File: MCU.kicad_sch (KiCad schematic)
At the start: 24 parts, among them J5 Micro_SD_Card, U4 EFM32GG332, Y1 Crystal_GND23

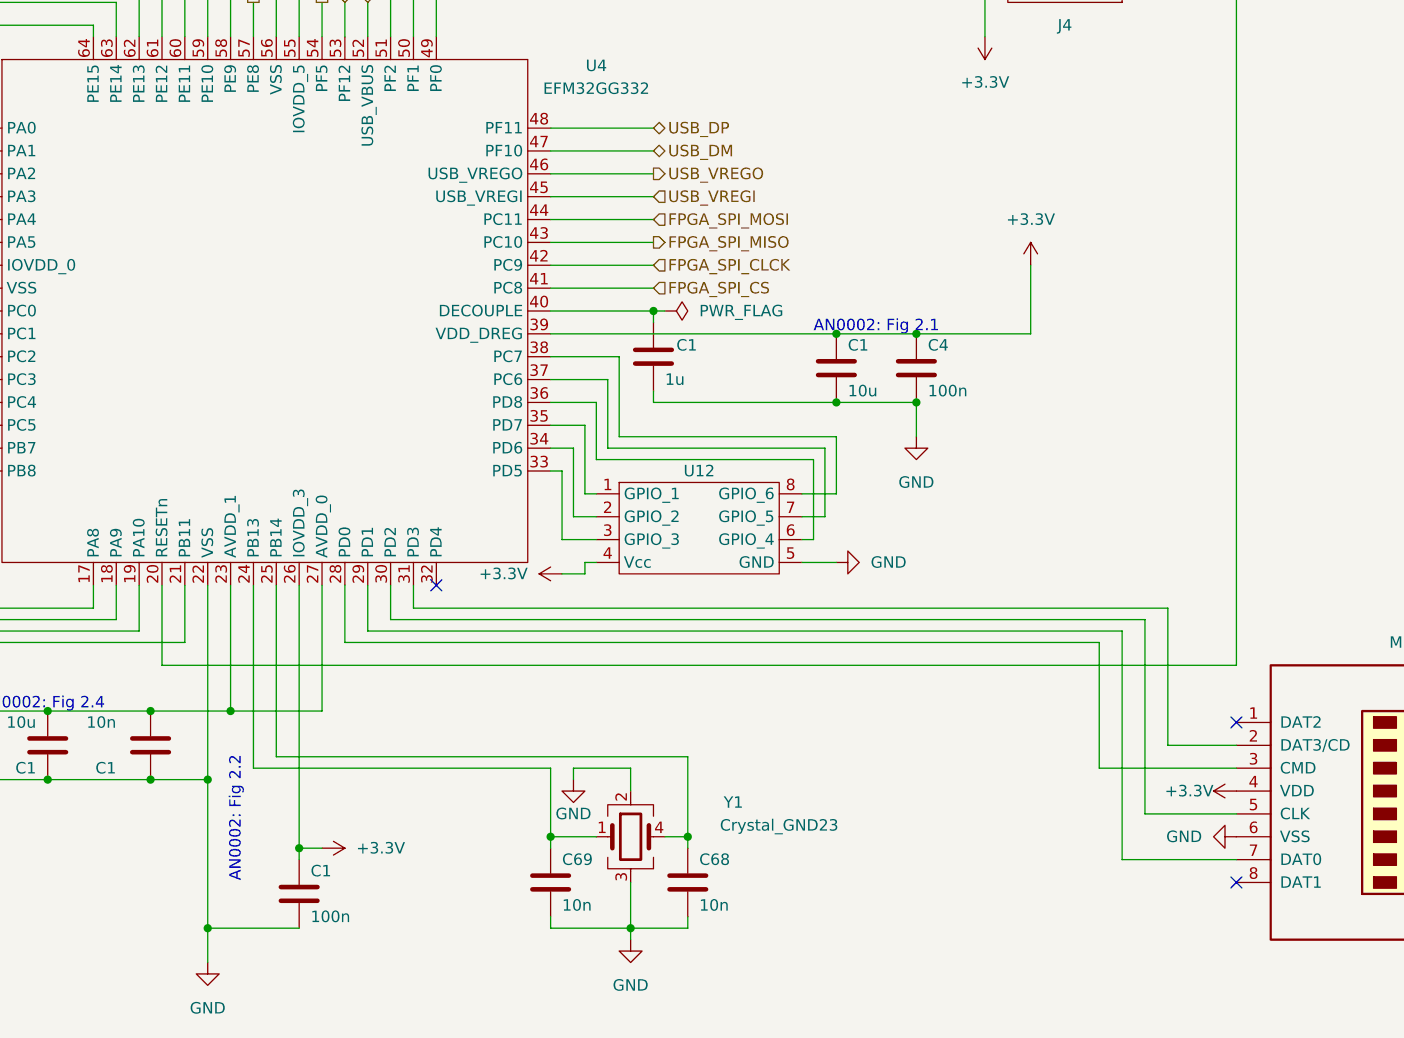
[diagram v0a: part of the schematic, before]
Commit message: Added Pullup resistors
And disconnected unused USB_volt ports
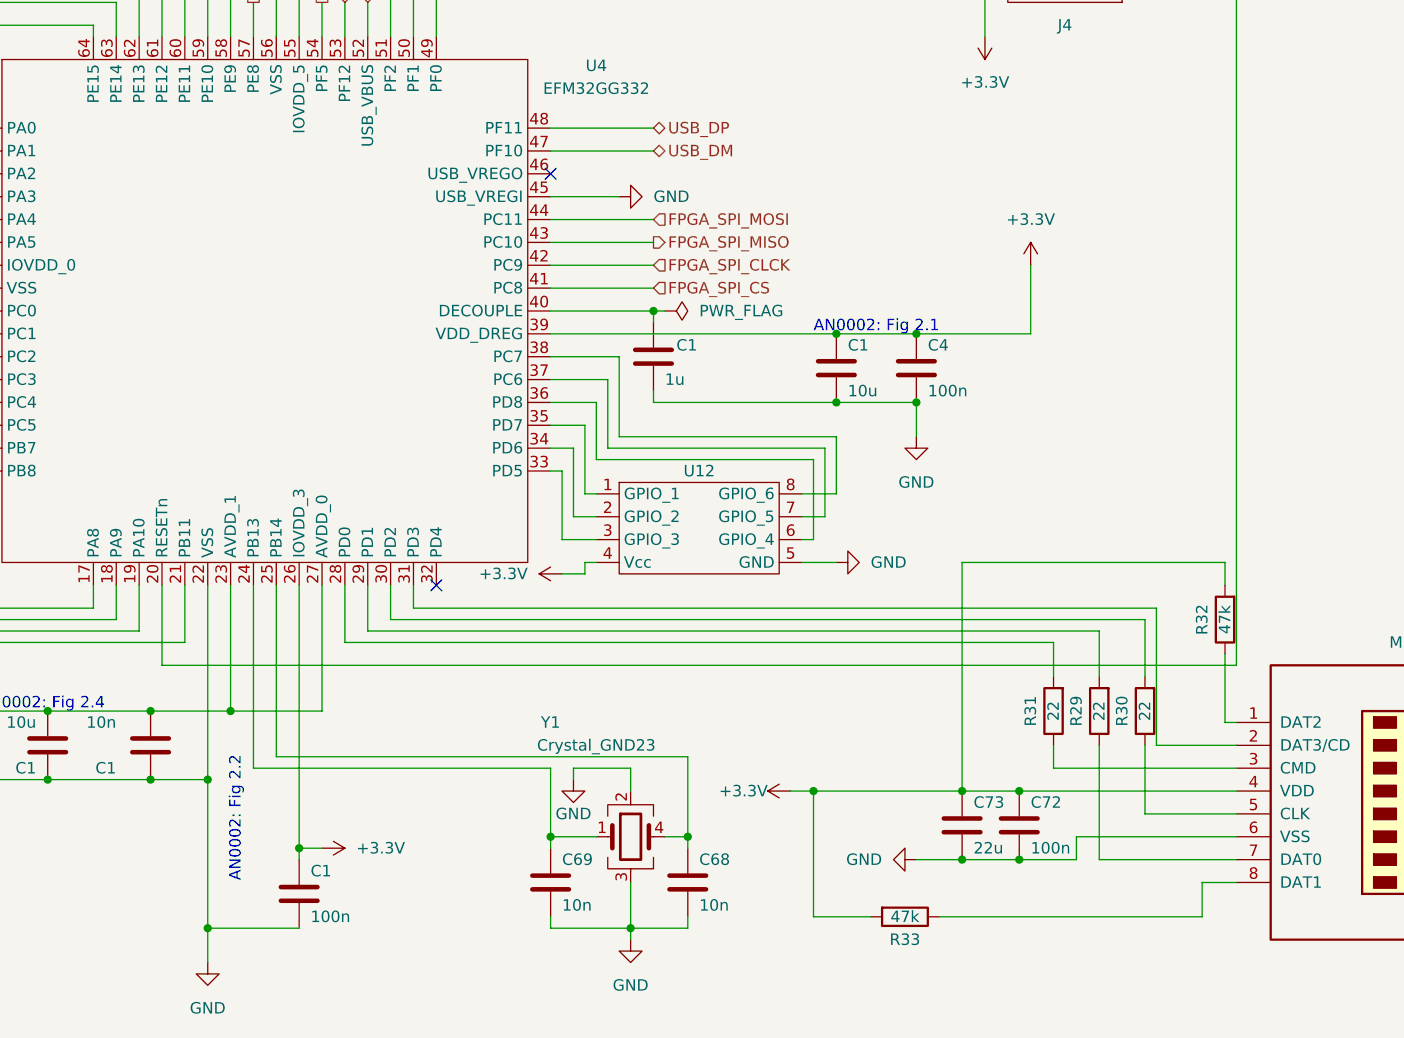
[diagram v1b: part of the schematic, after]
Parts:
- added C72: 100n, symbol Device:C
- added C73: 22u, symbol Device:C
- added R29, R30, R31: 22, symbol Device:R
- added R32, R33: 47k, symbol Device:R
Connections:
- net USB_VREGI is gone; now on net GND: U4.45 (USB_VREGI)
- net +3.3V: now also C72.1, C73.1, R32.2, R33.2
- net GND: now also C72.2, C73.2
- net at U4.28 (PD0): now also R31.2; no longer J5.3 (CMD)
- net at J5.7 (DAT0): now also R29.1; no longer U4.29 (PD1)
- net at U4.30 (PD2): now also R30.2; no longer J5.5 (CLK)
- net at J5.1 (DAT2): now also R32.1
- net at J5.8 (DAT1): now also R33.1
- net USB_VREGO: no longer names the net of U4.46 (USB_VREGO)
- new net: R29.2, U4.29 (PD1)
- new net: R21.1, U11.2 (R4), U13.2 (R4)
- new net: J5.3 (CMD), R31.1
- new net: J5.5 (CLK), R30.1
- no-connect marks 3 -> 2

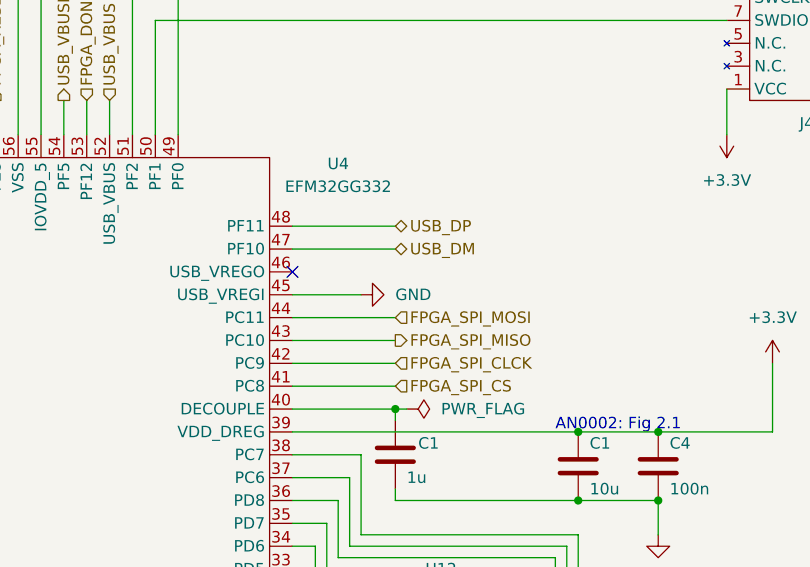
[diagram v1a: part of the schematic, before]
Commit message: Fixed mistake in USB_A connection
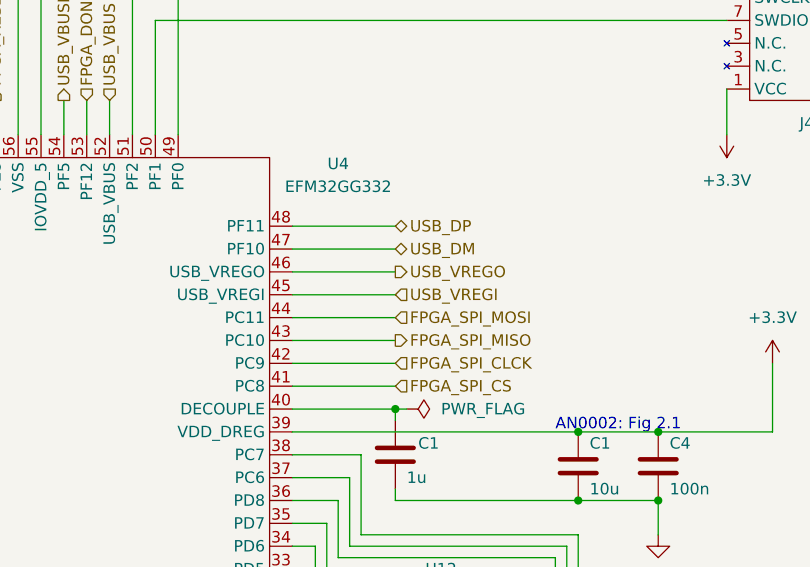
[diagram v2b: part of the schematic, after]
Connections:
- net GND: no longer U4.45 (USB_VREGI)
- net USB_VREGO: now reaches U4.46 (USB_VREGO)
- new net: R21.1, U11.2 (R4), U13.2 (R4)
- new net USB_VREGI: U4.45 (USB_VREGI)
- no-connect marks 2 -> 1
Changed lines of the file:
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@@
   )
   (no_connect (at 149.86 124.46))
-  (no_connect (at 162.56 78.74))
   (wire (pts (xy 46.99 113.03) (xy 63.5 113.03))
     (stroke (width 0) (type default))
@@
     (stroke (width 0) (type default))
   )
-  (wire (pts (xy 162.56 81.28) (xy 170.18 81.28))
+  (wire (pts (xy 162.56 81.28) (xy 173.99 81.28))
     (stroke (width 0) (type default))
   )
@@
   )
   (wire (pts (xy 134.62 153.67) (xy 134.62 154.94))
+    (stroke (width 0) (type default))
+  )
+  (wire (pts (xy 162.56 78.74) (xy 173.99 78.74))
     (stroke (width 0) (type default))
   )
@@
     (effects (font (size 1.27 1.27)) (justify left))
   )
+  (hierarchical_label "USB_VREGI" (shape input) (at 173.99 81.28 0) (fields_autoplaced)
+    (effects (font (size 1.27 1.27)) (justify left))
+  )
   (hierarchical_label "FPGA_RESET" (shape output) (at 129.54 59.69 90) (fields_autoplaced)
     (effects (font (size 1.27 1.27)) (justify left))
@@
   (hierarchical_label "Button 3" (shape input) (at 93.98 78.74 180) (fields_autoplaced)
     (effects (font (size 1.27 1.27)) (justify right))
+  )
+  (hierarchical_label "USB_VREGO" (shape output) (at 173.99 78.74 0) (fields_autoplaced)
+    (effects (font (size 1.27 1.27)) (justify left))
   )
   (hierarchical_label "FPGA_SPI_MOSI" (shape input) (at 173.99 83.82 0) (fields_autoplaced)
@@
         )
       )
-    )
-  )
-  (symbol (lib_id "power:GND") (at 170.18 81.28 90) (unit 1)
-    (in_bom yes) (on_board yes) (dnp no) (fields_autoplaced)
-    (property "Reference" "#PWR061" (at 176.53 81.28 0)
-      (effects (font (size 1.27 1.27)) hide)
-    )
-    (property "Value" "GND" (at 173.99 81.28 90)
-      (effects (font (size 1.27 1.27)) (justify right))
-    )
-    (property "Footprint" "" (at 170.18 81.28 0)
-      (effects (font (size 1.27 1.27)) hide)
-    )
-    (property "Datasheet" "" (at 170.18 81.28 0)
-      (effects (font (size 1.27 1.27)) hide)
-    )
-    (pin "1")
-    (instances
-      (project "GuitarZero"
-        (path "/fba50eda-8593-4456-af98-ff56fd418a76/ae46c600-e32c-45ef-b9ae-c42d4bac8718"
-          (reference "#PWR061") (unit 1)
-        )
-      )

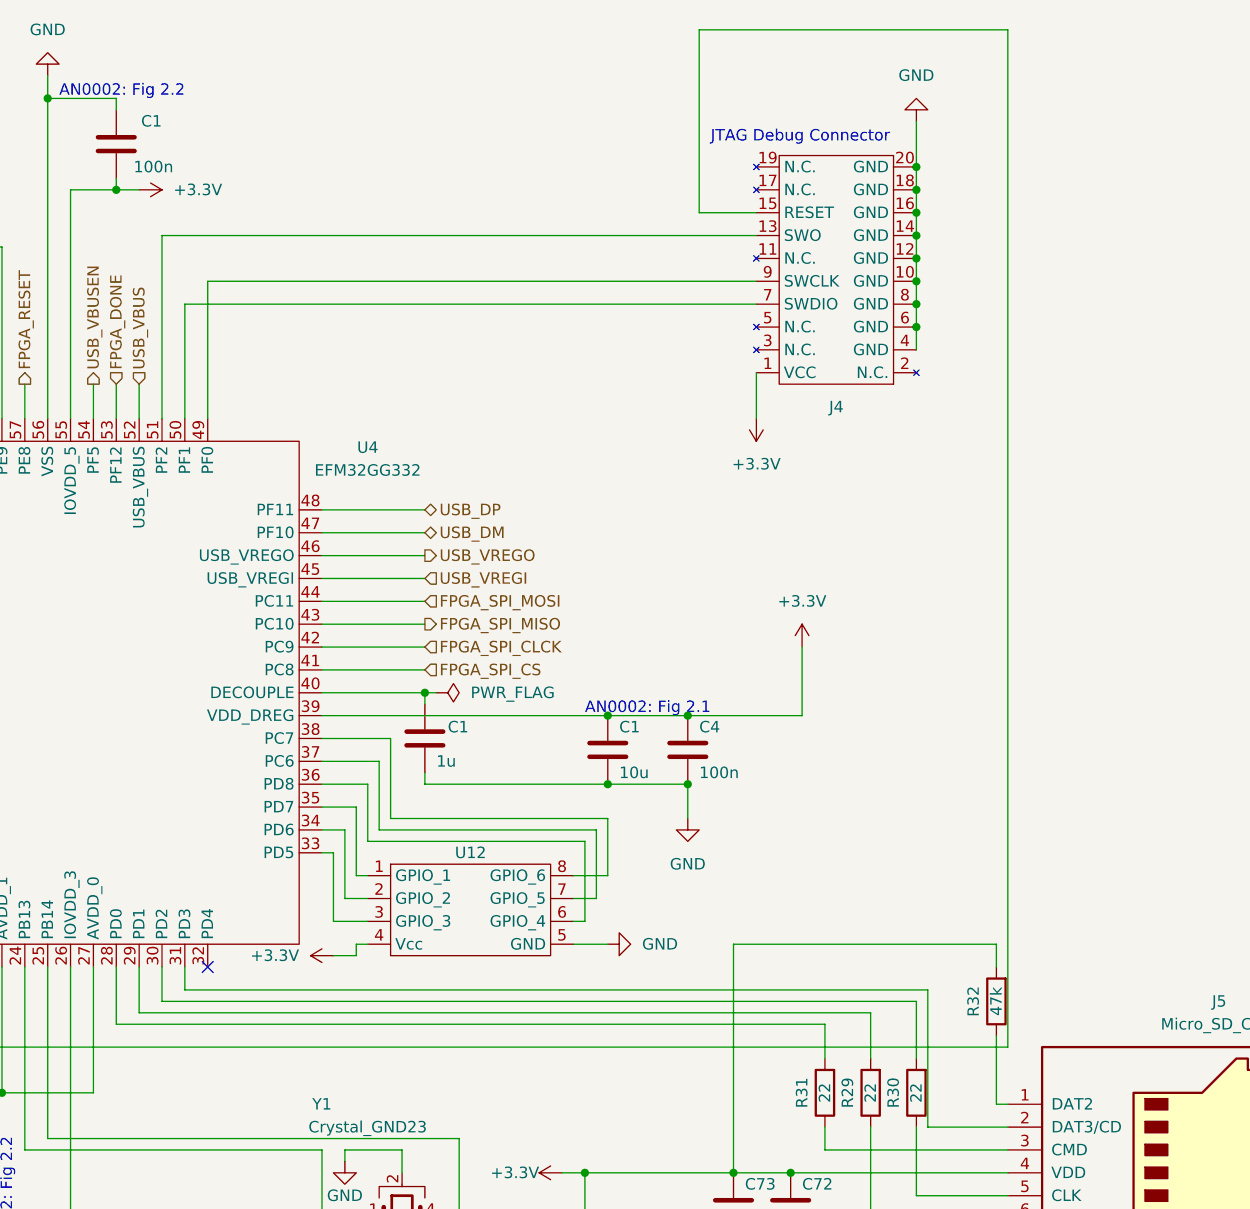
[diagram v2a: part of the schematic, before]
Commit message: Corrected MCU Debug pin
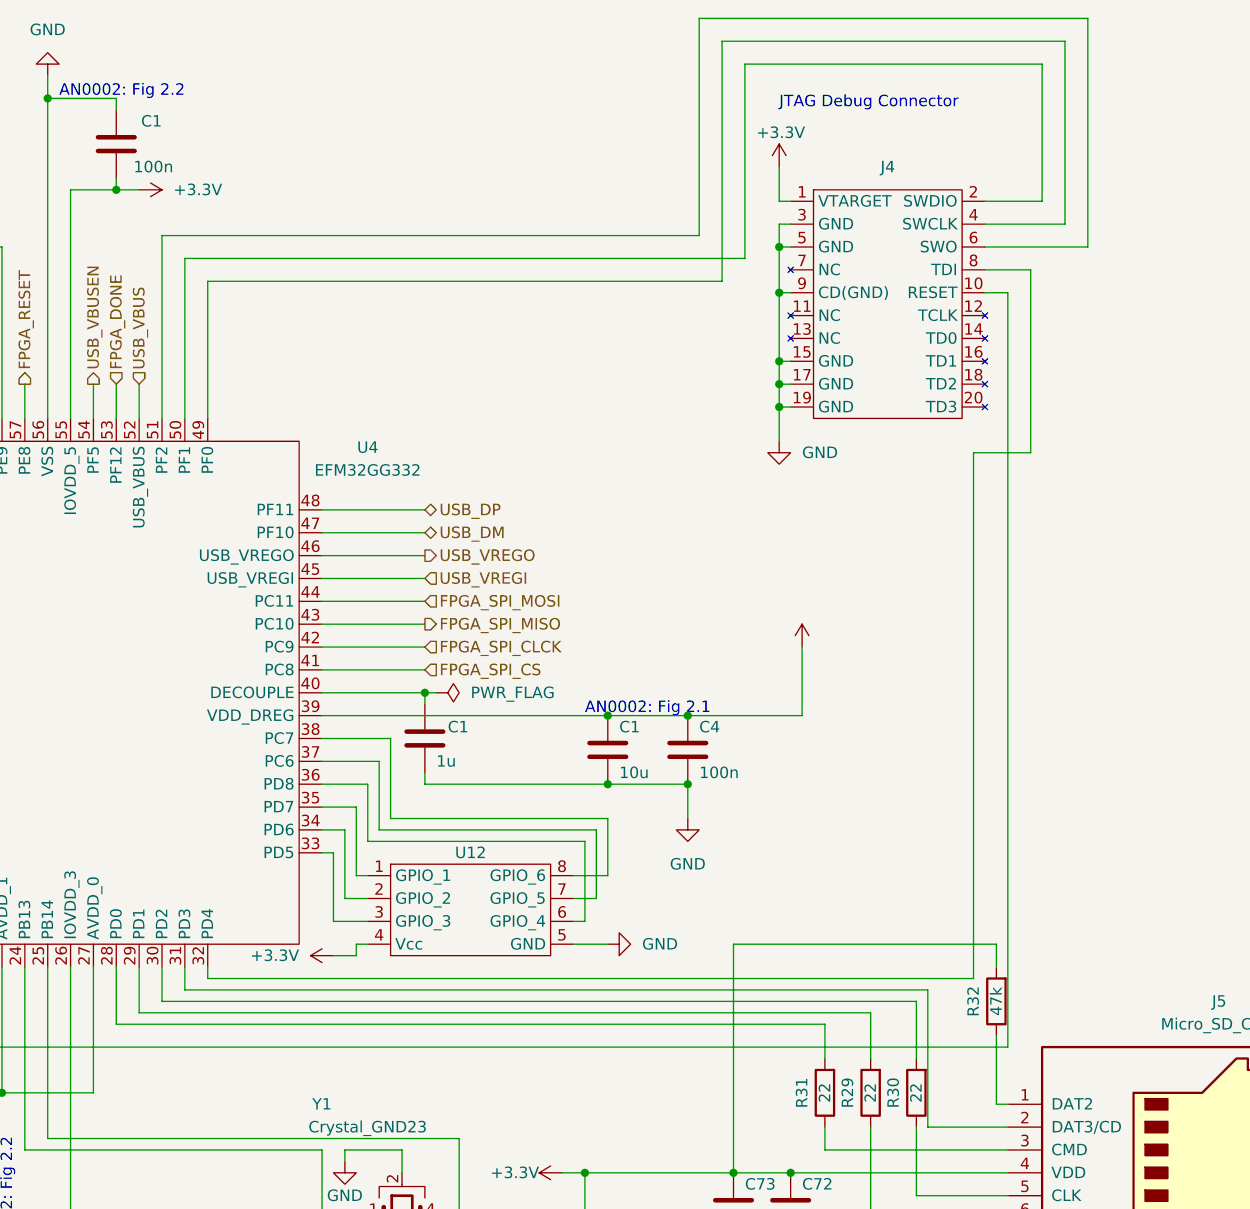
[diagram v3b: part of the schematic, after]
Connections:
- net GND: now also J4.15 (GND), J4.17 (GND), J4.19 (GND), J4.3 (GND), J4.5 (GND), J4.9 (CD(GND)); no longer J4.10 (GND), J4.12 (GND), J4.14 (GND), J4.16 (GND), J4.18 (GND), J4.20 (GND), J4.4 (GND), J4.6 (GND), J4.8 (GND)
- net at U4.51 (PF2): now also J4.6 (SWO); no longer J4.13 (SWO)
- net at U4.20 (RESETn): now also J4.10 (RESET); no longer J4.15 (RESET)
- net at J4.2 (SWDIO): now also U4.50 (PF1)
- net at J4.7 (NC): no longer U4.50 (PF1)
- net at U4.49 (PF0): now also J4.4 (SWCLK); no longer J4.9 (SWCLK)
- net at U4.32 (PD4): now also J4.8 (TDI)
- new net: R21.1, U11.2 (R4), U13.2 (R4)
- no-connect marks 1 -> 0

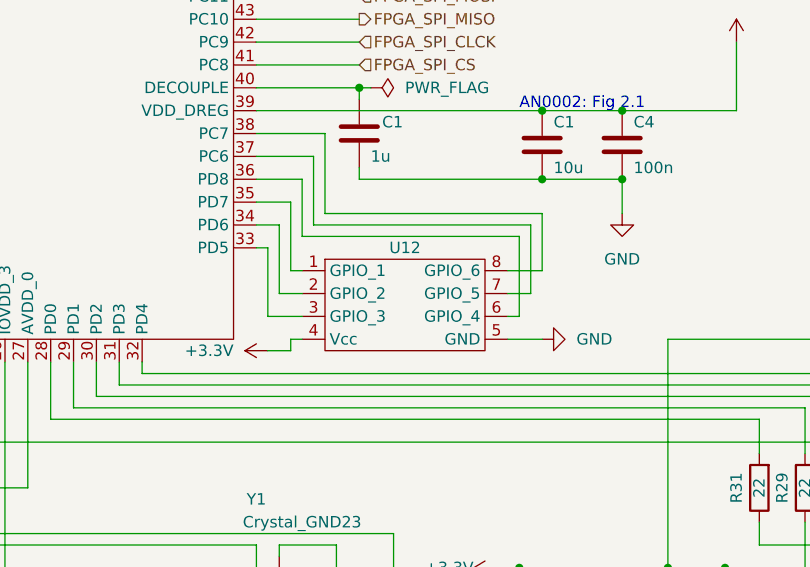
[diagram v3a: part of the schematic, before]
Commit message: Fixed PSU Jumper connection
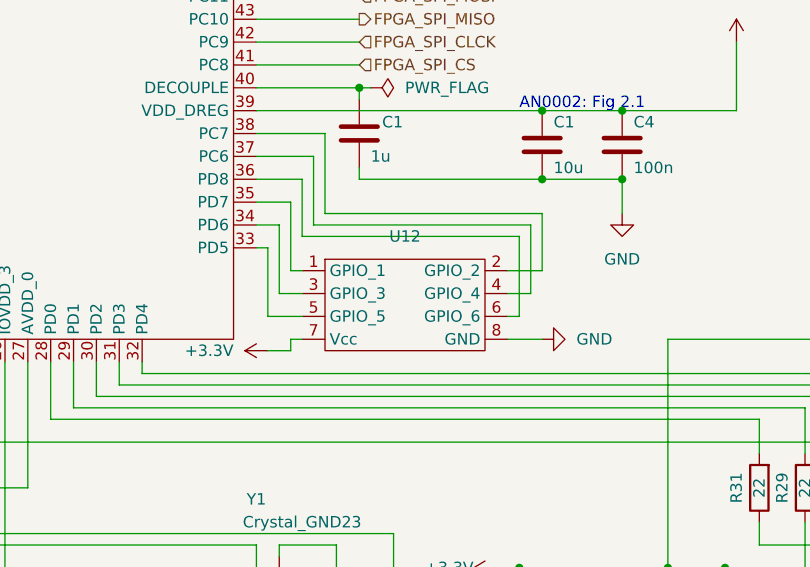
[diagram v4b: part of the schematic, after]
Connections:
- net +3.3V: now also U12.7 (Vcc); no longer U12.4 (Vcc)
- net GND: now also U12.8 (GND); no longer U12.5 (GND)
- net at U12.3 (GPIO_3): now also U4.34 (PD6); no longer U4.33 (PD5)
- net at U12.2 (GPIO_2): now also U4.38 (PC7); no longer U4.34 (PD6)
- net at U4.37 (PC6): now also U12.4 (GPIO_4); no longer U12.7 (GPIO_5)
- new net: U12.5 (GPIO_5), U4.33 (PD5)
- new net: R21.1, U11.2 (R4), U13.2 (R4)
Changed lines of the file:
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@@
     (effects (font (size 1.27 1.27)) (justify right))
+  )
+  (symbol (lib_id "GuitarZero:MCU_GPIO_Pins") (at 179.07 118.11 0) (unit 1)
+    (in_bom yes) (on_board yes) (dnp no) (fields_autoplaced)
+    (property "Reference" "U12" (at 179.07 110.49 0)
+      (effects (font (size 1.27 1.27)))
+    )
+    (property "Value" "~" (at 175.26 118.11 0)
+      (effects (font (size 1.27 1.27)))
+    )
+    (property "Footprint" "" (at 175.26 118.11 0)
+      (effects (font (size 1.27 1.27)) hide)
+    )
+    (property "Datasheet" "" (at 175.26 118.11 0)
+      (effects (font (size 1.27 1.27)) hide)
+    )
+    (pin "1")
+    (pin "2")
+    (pin "3")
+    (pin "4")
+    (pin "5")
+    (pin "6")
+    (pin "7")
+    (pin "8")
+    (instances
+      (project "GuitarZero"
+        (path "/fba50eda-8593-4456-af98-ff56fd418a76/ae46c600-e32c-45ef-b9ae-c42d4bac8718"
+          (reference "U12") (unit 1)
+        )
+      )
+    )
   )
   (symbol (lib_id "Device:R") (at 67.31 133.35 90) (unit 1)
@@
         )
       )
-    )
-  )
-  (symbol (lib_id "GuitarZero:MCU_GPIO_Pins") (at 179.07 118.11 0) (unit 1)
-    (in_bom yes) (on_board yes) (dnp no)
-    (property "Reference" "U12" (at 179.07 111.76 0)
-      (effects (font (size 1.27 1.27)))
-    )
-    (property "Value" "~" (at 175.26 118.11 0)
-      (effects (font (size 1.27 1.27)))
-    )
-    (property "Footprint" "" (at 175.26 118.11 0)
-      (effects (font (size 1.27 1.27)) hide)
-    )
-    (property "Datasheet" "" (at 175.26 118.11 0)
-      (effects (font (size 1.27 1.27)) hide)
-    )
-    (pin "1")
-    (pin "2")
-    (pin "3")
-    (pin "4")
-    (pin "5")
-    (pin "6")
-    (pin "7")
-    (pin "8")
-    (instances
-      (project "GuitarZero"
-        (path "/fba50eda-8593-4456-af98-ff56fd418a76/ae46c600-e32c-45ef-b9ae-c42d4bac8718"
-          (reference "U12") (unit 1)
-        )
-      )

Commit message: Made resistor values uniform
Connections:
- new net: R21.1, U11.2 (R4), U13.2 (R4)
